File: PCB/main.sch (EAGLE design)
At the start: 12 parts, among them X1 BU-SMA-V

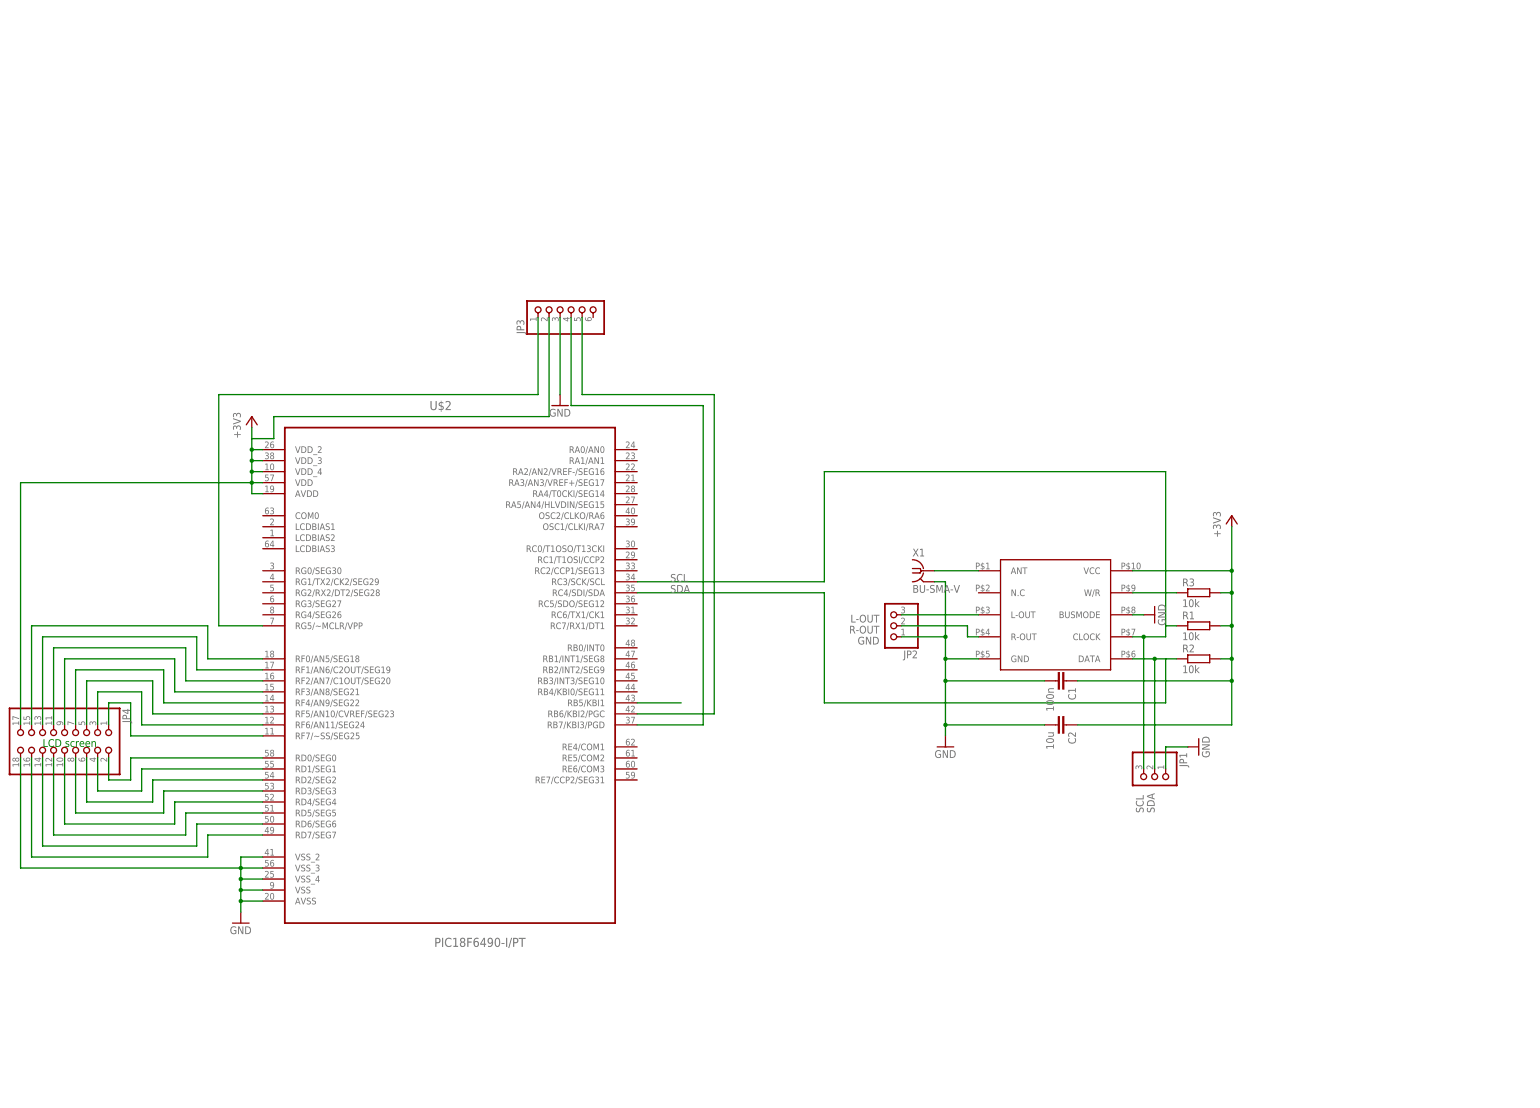
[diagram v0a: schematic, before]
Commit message: More schematic.
Added complete PIC breakout headers.
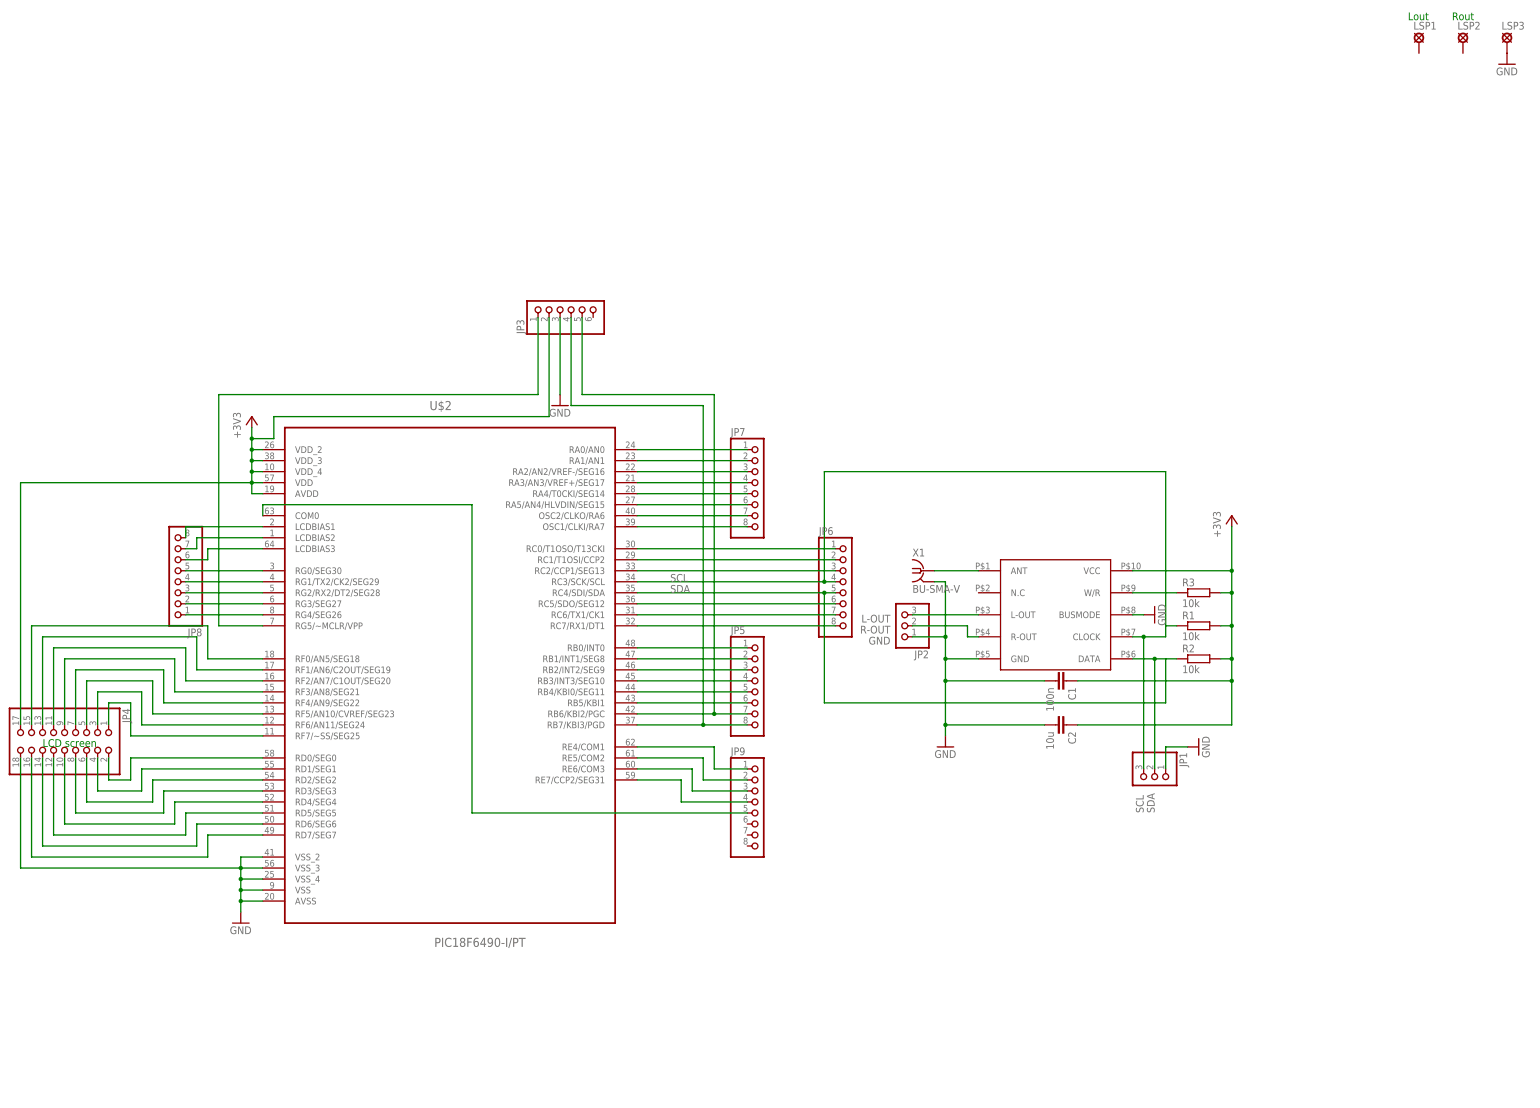
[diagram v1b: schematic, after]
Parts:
- added JP5, JP6, JP7, JP8, JP9: (no value), pinhead:PINHD-1X8
- added LSP1, LSP2, LSP3: LSP10, solpad:LSP10
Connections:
- new net N$23: JP6.8, U$2.RC7/RX1/DT1
- new net N$24: JP6.7, U$2.RC6/TX1/CK1
- new net N$25: JP5.5, U$2.RB4/KBI0/SEG11
- new net N$26: JP5.4, U$2.RB3/INT3/SEG10
- new net N$27: JP5.3, U$2.RB2/INT2/SEG9
- new net N$28: JP5.2, U$2.RB1/INT1/SEG8
- new net N$29: JP5.1, U$2.RB0/INT0
- new net N$30: JP6.6, U$2.RC5/SDO/SEG12
- new net N$31: JP6.3, U$2.RC2/CCP1/SEG13
- new net N$32: JP6.2, U$2.RC1/T1OSI/CCP2
- new net N$33: JP6.1, U$2.RC0/T1OSO/T13CKI
- new net N$34: JP7.8, U$2.OSC1/CLKI/RA7
- new net N$35: JP7.7, U$2.OSC2/CLKO/RA6
- new net N$36: JP7.6, U$2.RA5/AN4/HLVDIN/SEG15
- new net N$37: JP7.5, U$2.RA4/T0CKI/SEG14
- new net N$38: JP7.4, U$2.RA3/AN3/VREF+/SEG17
- new net N$39: JP7.3, U$2.RA2/AN2/VREF-/SEG16
- new net N$40: JP7.2, U$2.RA1/AN1
- new net N$41: JP7.1, U$2.RA0/AN0
- new net N$42: JP8.1, U$2.RG4/SEG26
- new net N$43: JP8.2, U$2.RG3/SEG27
- new net N$44: JP8.3, U$2.RG2/RX2/DT2/SEG28
- new net N$45: JP8.4, U$2.RG1/TX2/CK2/SEG29
- new net N$46: JP8.5, U$2.RG0/SEG30
- new net N$47: JP8.6, U$2.LCDBIAS3
- new net N$48: JP8.7, U$2.LCDBIAS2
- new net N$49: JP8.8, U$2.LCDBIAS1
- new net N$50: JP9.1, U$2.RE4/COM1
- new net N$51: JP9.2, U$2.RE5/COM2
- new net N$52: JP9.3, U$2.RE6/COM3
- new net N$53: JP9.4, U$2.RE7/CCP2/SEG31
- new net N$54: JP9.5, U$2.COM0
- net GND: now also LSP3.MP
- net N$10: now also JP5.7
- net N$11: now also JP5.8
- net N$9: now also JP5.6
- net SCL: now also JP6.4
- net SDA: now also JP6.5
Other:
- note added: "Lout"
- note added: "Rout"
- moved on the sheet: JP2

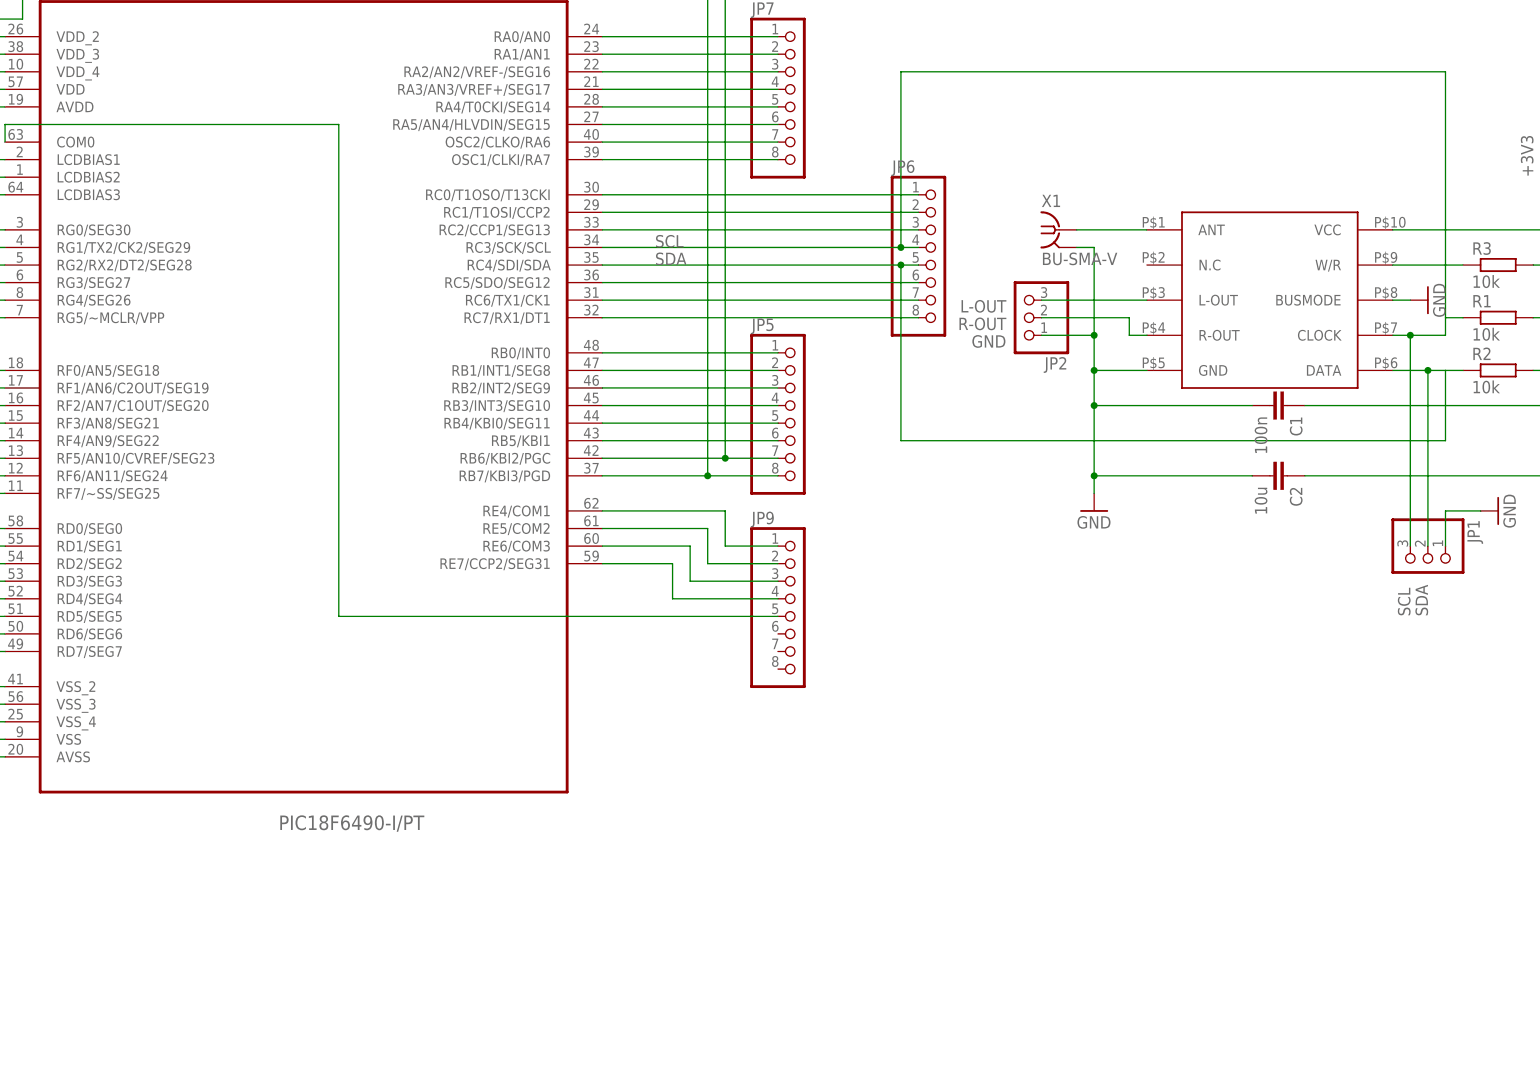
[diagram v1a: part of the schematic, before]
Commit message: Yet more schematic.
Added voltage regulator.
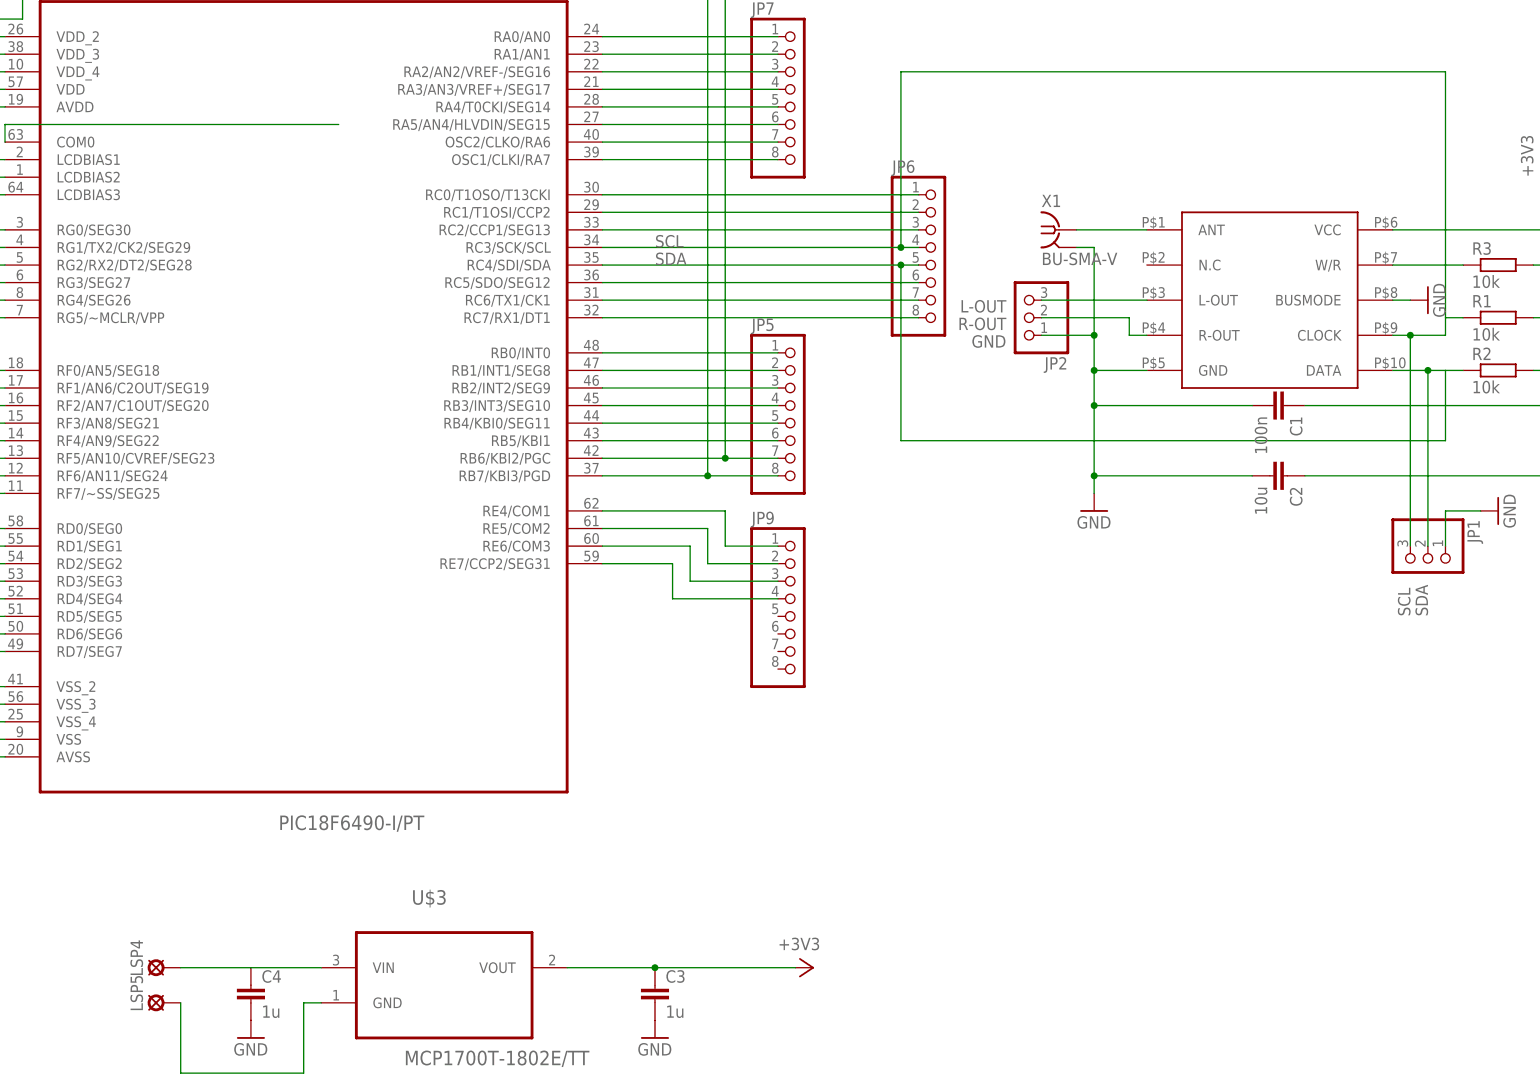
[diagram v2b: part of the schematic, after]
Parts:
- added C3, C4: 1u, rcl:C-EUC0805
- added LSP4, LSP5: LSP11, solpad:LSP11
- added U$3: MCP1700T-1802E/TT, mcp1700t-vreg:MCP1700T-1802E/TT
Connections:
- new net N$55: C4.1, LSP4.MP, U$3.VIN
- new net N$56: LSP5.MP, U$3.GND
- net +3V3: now also C3.1, U$3.VOUT
- net GND: now also C3.2, C4.2
- net N$54: no longer JP9.5
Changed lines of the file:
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@@
 <part name="JP8" library="pinhead" deviceset="PINHD-1X8" device=""/>
 <part name="JP9" library="pinhead" deviceset="PINHD-1X8" device=""/>
+<part name="U$3" library="mcp1700t-vreg" deviceset="MCP1700T-1802E/TT" device=""/>
+<part name="+3V3" library="supply1" deviceset="+3V3" device=""/>
+<part name="LSP4" library="solpad" deviceset="LSP11" device=""/>
+<part name="LSP5" library="solpad" deviceset="LSP11" device=""/>
+<part name="C3" library="rcl" deviceset="C-EU" device="C0805" value="1u"/>
+<part name="GND7" library="supply1" deviceset="GND" device=""/>
+<part name="GND8" library="supply1" deviceset="GND" device=""/>
+<part name="C4" library="rcl" deviceset="C-EU" device="C0805" value="1u"/>
 </parts>
 <sheets>
@@
 <instance part="JP8" gate="A" x="81.28" y="96.52" rot="R180"/>
 <instance part="JP9" gate="A" x="215.9" y="40.64"/>
+<instance part="U$3" gate="A" x="165.1" y="-10.16"/>
+<instance part="+3V3" gate="G$1" x="218.44" y="-10.16" rot="R270"/>
+<instance part="LSP4" gate="1" x="124.46" y="-10.16" rot="R90"/>
+<instance part="LSP5" gate="1" x="124.46" y="-15.24" rot="R90"/>
+<instance part="C3" gate="G$1" x="195.58" y="-12.7"/>
+<instance part="GND7" gate="1" x="195.58" y="-20.32"/>
+<instance part="GND8" gate="1" x="137.16" y="-20.32"/>
+<instance part="C4" gate="G$1" x="137.16" y="-12.7"/>
 </instances>
 <busses>
@@
 <junction x="99.06" y="127"/>
 </segment>
+<segment>
+<pinref part="U$3" gate="A" pin="VOUT"/>
+<pinref part="+3V3" gate="G$1" pin="+3V3"/>
+<wire x1="215.9" y1="-10.16" x2="195.58" y2="-10.16" width="0.1524" layer="91"/>
+<pinref part="C3" gate="G$1" pin="1"/>
+<wire x1="195.58" y1="-10.16" x2="182.88" y2="-10.16" width="0.1524" layer="91"/>
+<junction x="195.58" y="-10.16"/>
+</segment>
 </net>
 <net name="GND" class="0">
@@
 <pinref part="GND6" gate="1" pin="GND"/>
 </segment>
+<segment>
+<pinref part="C3" gate="G$1" pin="2"/>
+<pinref part="GND7" gate="1" pin="GND"/>
+</segment>
+<segment>
+<pinref part="C4" gate="G$1" pin="2"/>
+<pinref part="GND8" gate="1" pin="GND"/>
+</segment>
 </net>
 <net name="N$4" class="0">
@@
 <wire x1="101.6" y1="109.22" x2="101.6" y2="111.76" width="0.1524" layer="91"/>
 <wire x1="101.6" y1="111.76" x2="149.86" y2="111.76" width="0.1524" layer="91"/>
-<pinref part="JP9" gate="A" pin="5"/>
-<wire x1="149.86" y1="111.76" x2="149.86" y2="40.64" width="0.1524" layer="91"/>
-<wire x1="149.86" y1="40.64" x2="213.36" y2="40.64" width="0.1524" layer="91"/>
-</segment>
-</net>
+</segment>
+</net>
+<net name="N$55" class="0">
+<segment>
+<pinref part="U$3" gate="A" pin="VIN"/>
+<wire x1="147.32" y1="-10.16" x2="137.16" y2="-10.16" width="0.1524" layer="91"/>
+<pinref part="C4" gate="G$1" pin="1"/>
+<pinref part="LSP4" gate="1" pin="MP"/>
+<wire x1="137.16" y1="-10.16" x2="127" y2="-10.16" width="0.1524" layer="91"/>
+</segment>
+</net>
+<net name="N$56" class="0">
+<segment>
+<pinref part="LSP5" gate="1" pin="MP"/>
+<wire x1="127" y1="-15.24" x2="127" y2="-25.4" width="0.1524" layer="91"/>
+<wire x1="127" y1="-25.4" x2="144.78" y2="-25.4" width="0.1524" layer="91"/>
+<pinref part="U$3" gate="A" pin="GND"/>
+<wire x1="144.78" y1="-25.4" x2="144.78" y2="-15.24" width="0.1524" layer="91"/>
+<wire x1="144.78" y1="-15.24" x2="147.32" y2="-15.24" width="0.1524" layer="91"/>
+</segment>
+</net>
